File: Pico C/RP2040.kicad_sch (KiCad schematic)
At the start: 16 parts, among them U1 RP2040

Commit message: Add files via upload
Upload boardview file for use with OpenBoardView.
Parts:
- C10, C11, C4, C5, C6, C7, C8, C9: footprint Capacitor_SMD:C_0201_0603Metric -> Pico_C:C_0201_0603Metric
- R14, R15: footprint Resistor_SMD:R_0201_0603Metric -> Pico_C:R_0201_0603Metric
- U1: footprint Pico_C:QFN-56-1EP_7x7mm_P0.4mm_EP3.2x3.2mm -> Pico_C:QFN-56-1EP_7x7mm_P0.4mm_EP3.2x3.2mm_ThermalVias
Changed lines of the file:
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@@
       (effects (font (size 1.27 1.27)) (justify left))
     )
-    (property "Footprint" "Capacitor_SMD:C_0201_0603Metric" (at 211.1502 43.18 0)
+    (property "Footprint" "Pico_C:C_0201_0603Metric" (at 211.1502 43.18 0)
       (effects (font (size 1.27 1.27)) hide)
     )
@@
       (effects (font (size 1.27 1.27)) (justify left))
     )
-    (property "Footprint" "Capacitor_SMD:C_0201_0603Metric" (at 186.3852 43.18 0)
+    (property "Footprint" "Pico_C:C_0201_0603Metric" (at 186.3852 43.18 0)
       (effects (font (size 1.27 1.27)) hide)
     )
@@
       (effects (font (size 1.27 1.27)) (justify left))
     )
-    (property "Footprint" "Capacitor_SMD:C_0201_0603Metric" (at 87.9602 43.815 0)
+    (property "Footprint" "Pico_C:C_0201_0603Metric" (at 87.9602 43.815 0)
       (effects (font (size 1.27 1.27)) hide)
     )
@@
       (effects (font (size 1.27 1.27)) (justify left))
     )
-    (property "Footprint" "Capacitor_SMD:C_0201_0603Metric" (at 101.2952 43.815 0)
+    (property "Footprint" "Pico_C:C_0201_0603Metric" (at 101.2952 43.815 0)
       (effects (font (size 1.27 1.27)) hide)
     )
@@
       (effects (font (size 1.27 1.27)) (justify left))
     )
-    (property "Footprint" "Capacitor_SMD:C_0201_0603Metric" (at 199.0852 43.18 0)
+    (property "Footprint" "Pico_C:C_0201_0603Metric" (at 199.0852 43.18 0)
       (effects (font (size 1.27 1.27)) hide)
     )
@@
       (effects (font (size 1.27 1.27)) (justify left))
     )
-    (property "Footprint" "Capacitor_SMD:C_0201_0603Metric" (at 223.2152 43.18 0)
+    (property "Footprint" "Pico_C:C_0201_0603Metric" (at 223.2152 43.18 0)
       (effects (font (size 1.27 1.27)) hide)
     )
@@
       (effects (font (size 1.27 1.27)) (justify left))
     )
-    (property "Footprint" "Capacitor_SMD:C_0201_0603Metric" (at 234.0102 43.18 0)
+    (property "Footprint" "Pico_C:C_0201_0603Metric" (at 234.0102 43.18 0)
       (effects (font (size 1.27 1.27)) hide)
     )
@@
       (effects (font (size 1.27 1.27)) (justify left))
     )
-    (property "Footprint" "Pico_C:QFN-56-1EP_7x7mm_P0.4mm_EP3.2x3.2mm" (at 140.97 112.395 0)
+    (property "Footprint" "Pico_C:QFN-56-1EP_7x7mm_P0.4mm_EP3.2x3.2mm_ThermalVias" (at 140.97 112.395 0)
       (effects (font (size 1.27 1.27)) hide)
     )
@@
       (effects (font (size 1.27 1.27)) (justify left))
     )
-    (property "Footprint" "Capacitor_SMD:C_0201_0603Metric" (at 246.7102 43.18 0)
+    (property "Footprint" "Pico_C:C_0201_0603Metric" (at 246.7102 43.18 0)
       (effects (font (size 1.27 1.27)) hide)
     )
@@
       (effects (font (size 1.27 1.27)))
     )
-    (property "Footprint" "Resistor_SMD:R_0201_0603Metric" (at 102.489 83.439 90)
+    (property "Footprint" "Pico_C:R_0201_0603Metric" (at 102.489 83.439 90)
       (effects (font (size 1.27 1.27)) hide)
     )
@@
       (effects (font (size 1.27 1.27)))
     )
-    (property "Footprint" "Resistor_SMD:R_0201_0603Metric" (at 102.489 80.899 90)
-      (effects (font (size 1.27 1.27)) hide)
-    )
+    (property "Footprint" "Pico_C:R_0201_0603Metric" (at 102.489 80.899 90)
+      (effects (font (size 1.27 1.27)) hide)
+    )

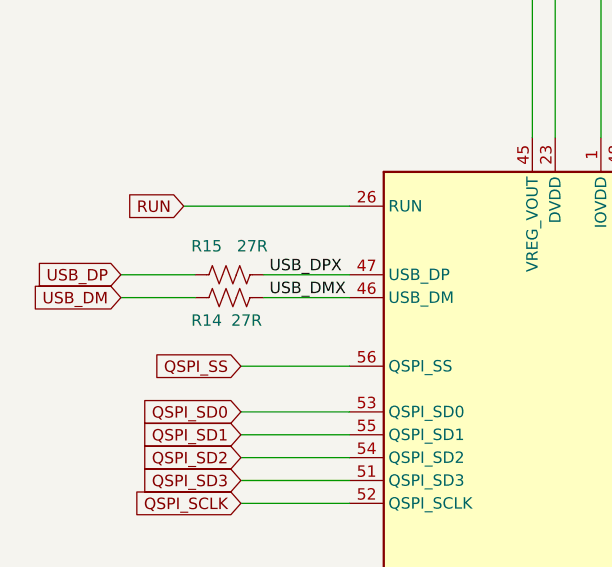
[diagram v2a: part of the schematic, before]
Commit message: Add files via upload
Updated component references to more closely match the original Pico.
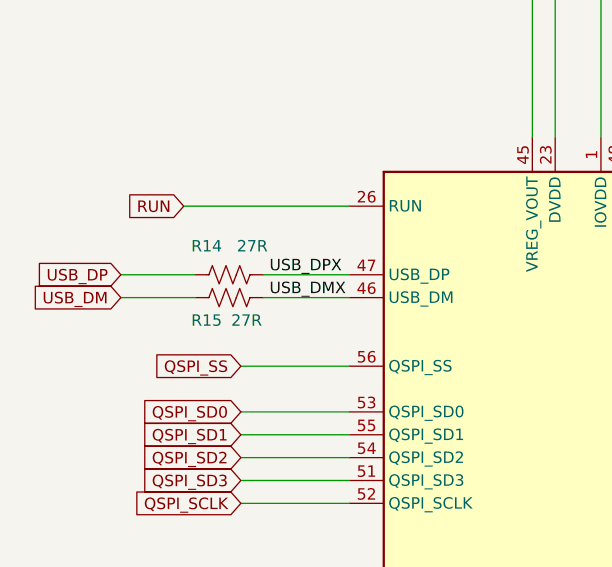
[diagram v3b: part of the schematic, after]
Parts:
- renumbered R15 to R14, R14 to R15
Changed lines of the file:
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@@
 		(on_board yes)
 		(dnp no)
-		(property "Reference" "R14"
+		(property "Reference" "R15"
 			(at 99.695 86.995 90)
 			(effects
@@
 			(project "RPI-PICO-R3a-PUBLIC"
 				(path "/f8a1033e-7d4e-4018-9b4c-1da5b150b31c/164d5e18-036f-432c-a221-4602efeaa5ef"
-					(reference "R14")
+					(reference "R15")
 					(unit 1)
 				)
@@
 		(on_board yes)
 		(dnp no)
-		(property "Reference" "R15"
+		(property "Reference" "R14"
 			(at 99.695 78.74 90)
 			(effects
@@
 			(project "RPI-PICO-R3a-PUBLIC"
 				(path "/f8a1033e-7d4e-4018-9b4c-1da5b150b31c/164d5e18-036f-432c-a221-4602efeaa5ef"
-					(reference "R15")
-					(unit 1)
-				)
+					(reference "R14")
+					(unit 1)
+				)

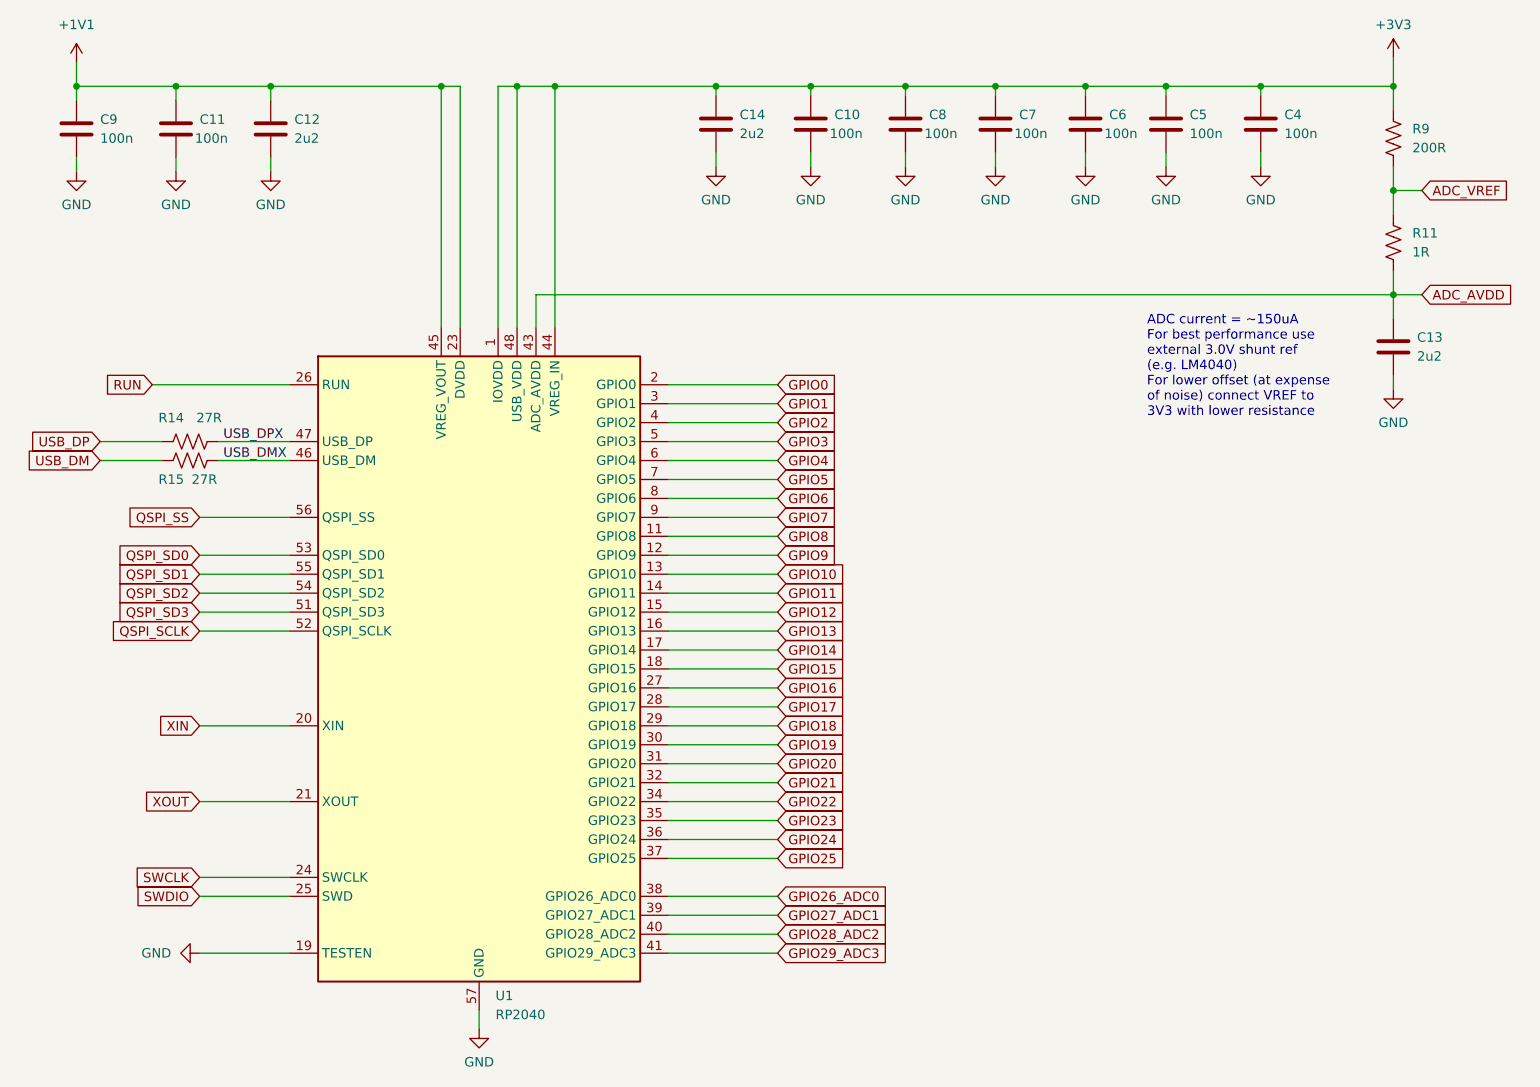
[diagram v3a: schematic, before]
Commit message: Add files via upload
Changed resistor reference numbers to match the real Pico H.
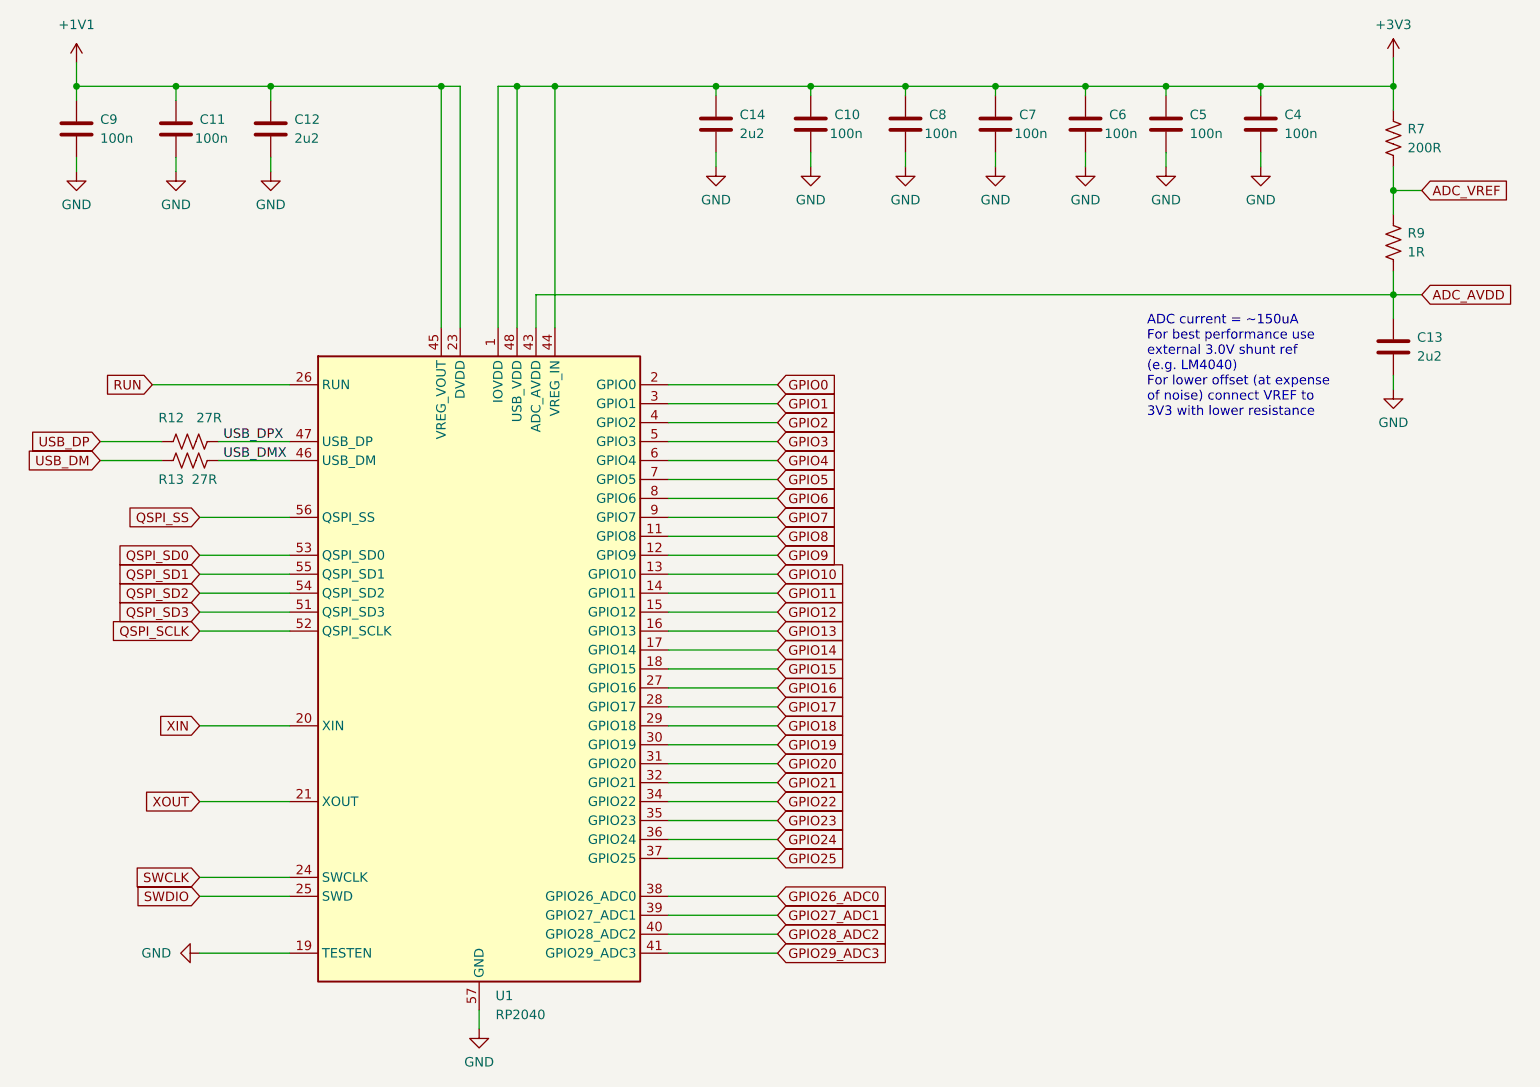
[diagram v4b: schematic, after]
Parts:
- renumbered R14 to R12, R15 to R13, R9 to R7, R11 to R9
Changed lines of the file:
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@@
 		(dnp no)
 		(fields_autoplaced yes)
-		(property "Reference" "R11"
-			(at 266.065 53.975 0)
+		(property "Reference" "R9"
+			(at 265.43 53.9749 0)
 			(effects
 				(font
@@
 		)
 		(property "Value" "1R"
-			(at 266.065 56.515 0)
+			(at 265.43 56.5149 0)
 			(effects
 				(font
@@
 			(project "RPI-PICO-R3a-PUBLIC"
 				(path "/f8a1033e-7d4e-4018-9b4c-1da5b150b31c/164d5e18-036f-432c-a221-4602efeaa5ef"
-					(reference "R11")
+					(reference "R9")
 					(unit 1)
 				)
@@
 		(dnp no)
 		(fields_autoplaced yes)
-		(property "Reference" "R9"
-			(at 266.065 40.005 0)
+		(property "Reference" "R7"
+			(at 265.43 40.0049 0)
 			(effects
 				(font
@@
 		)
 		(property "Value" "200R"
-			(at 266.065 42.545 0)
+			(at 265.43 42.5449 0)
 			(effects
 				(font
@@
 			(project "RPI-PICO-R3a-PUBLIC"
 				(path "/f8a1033e-7d4e-4018-9b4c-1da5b150b31c/164d5e18-036f-432c-a221-4602efeaa5ef"
-					(reference "R9")
+					(reference "R7")
 					(unit 1)
 				)
@@
 		(on_board yes)
 		(dnp no)
-		(property "Reference" "R15"
+		(property "Reference" "R13"
 			(at 99.695 86.995 90)
 			(effects
@@
 			(project "RPI-PICO-R3a-PUBLIC"
 				(path "/f8a1033e-7d4e-4018-9b4c-1da5b150b31c/164d5e18-036f-432c-a221-4602efeaa5ef"
-					(reference "R15")
+					(reference "R13")
 					(unit 1)
 				)
@@
 		(on_board yes)
 		(dnp no)
-		(property "Reference" "R14"
+		(property "Reference" "R12"
 			(at 99.695 78.74 90)
 			(effects
@@
 			(project "RPI-PICO-R3a-PUBLIC"
 				(path "/f8a1033e-7d4e-4018-9b4c-1da5b150b31c/164d5e18-036f-432c-a221-4602efeaa5ef"
-					(reference "R14")
-					(unit 1)
-				)
+					(reference "R12")
+					(unit 1)
+				)
